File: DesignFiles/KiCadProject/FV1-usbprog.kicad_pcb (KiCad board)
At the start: 2 copper layers, 36 x 32 mm, 8 parts, among them P1 PROG_BUF, U1 74LV4066, U2 CY7C68013A_dev_kit

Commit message: Updated to kicad 5.1, improved compatibility with newer FX2LP boards
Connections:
- U2 pad 10: GND -> Net-(U2-Pad10)
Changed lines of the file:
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@@
-(kicad_pcb (version 4) (host pcbnew "(2015-10-14 BZR 6269, Git 3ca8244)-product")
+(kicad_pcb (version 20171130) (host pcbnew "(5.1.4)-1")
   (general
-    (links 26)
-    (no_connects 0)
-    (area 161.849999 107.099999 198.650001 139.900001)
     (thickness 1.6)
     (drawings 33)
@@
     (zones 0)
     (modules 8)
-    (nets 44)
+    (nets 45)
   )
   (page A4)
@@
     (zone_45_only no)
     (trace_min 0.2)
-    (segment_width 0.2)
-    (edge_width 0.15)
     (via_size 1.6)
     (via_drill 0.6)
@@
     (uvia_min_size 0.2)
     (uvia_min_drill 0.1)
+    (edge_width 0.15)
+    (segment_width 0.2)
     (pcb_text_width 0.3)
     (pcb_text_size 1.5 1.5)
@@
       (layerselection 0x310f0_80000001)
       (usegerberextensions true)
+      (usegerberattributes false)
+      (usegerberadvancedattributes false)
+      (creategerberjobfile false)
       (excludeedgelayer true)
       (linewidth 0.200000)
@@
       (hpglpennumber 1)
       (hpglpenspeed 20)
-      (hpglpendiameter 15)
-      (hpglpenoverlay 2)
+      (hpglpendiameter 15.000000)
       (psnegative false)
       (psa4output false)
@@
       (drillshape 0)
       (scaleselection 1)
-      (outputdirectory I:/Electronics/Projects/Hardware/Gerbers/i2c_buffer/))
+      (outputdirectory "I:/Electronics/Projects/Hardware/Gerbers/i2c_buffer/"))
   )
   (net 0 "")
@@
   (net 42 "Net-(U1-Pad8)")
   (net 43 "Net-(U1-Pad10)")
+  (net 44 "Net-(U2-Pad10)")
   (net_class Default "This is the default net class."
     (clearance 0.25)
@@
     (add_net "Net-(U1-Pad8)")
     (add_net "Net-(U2-Pad1)")
+    (add_net "Net-(U2-Pad10)")
     (add_net "Net-(U2-Pad12)")
     (add_net "Net-(U2-Pad15)")
@@
       (effects (font (size 0.8 0.8) (thickness 0.15)))
     )
-    (fp_text value PROG_BUF (at 2.6 14.79 360) (layer F.Fab)
+    (fp_text value PROG_BUF (at 2.6 14.79) (layer F.Fab)
       (effects (font (size 0.8 0.8) (thickness 0.15)))
     )
@@
       (net 1 /TRG_PWR))
     (model Pin_Headers.3dshapes/Pin_Header_Angled_1x05.wrl
-      (at (xyz 0 -0.2 0))
+      (offset (xyz 0 -5.079999923706055 0))
       (scale (xyz 1 1 1))
       (rotate (xyz 0 0 90))
@@
       (net 2 GND))
     (pad 10 thru_hole circle (at 2.54 10.16) (size 1.8 1.8) (drill 1) (layers *.Cu *.Mask F.SilkS)
-      (net 2 GND))
+      (net 44 "Net-(U2-Pad10)"))
     (pad 11 thru_hole circle (at 0 12.7) (size 1.8 1.8) (drill 1) (layers *.Cu *.Mask F.SilkS)
       (net 2 GND))
@@
       (net 2 GND))
     (model Capacitors_ThroughHole.3dshapes/C_Disc_D3_P2.5.wrl
-      (at (xyz 0.0492126 0 0))
+      (offset (xyz 1.250000021226883 0 0))
       (scale (xyz 1 1 1))
       (rotate (xyz 0 0 0))
@@
     (tags R)
     (autoplace_cost180 10)
-    (fp_text reference R1 (at -1.75 -2 360) (layer F.SilkS)
+    (fp_text reference R1 (at -1.75 -2) (layer F.SilkS)
       (effects (font (size 0.8 0.8) (thickness 0.2032)))
     )

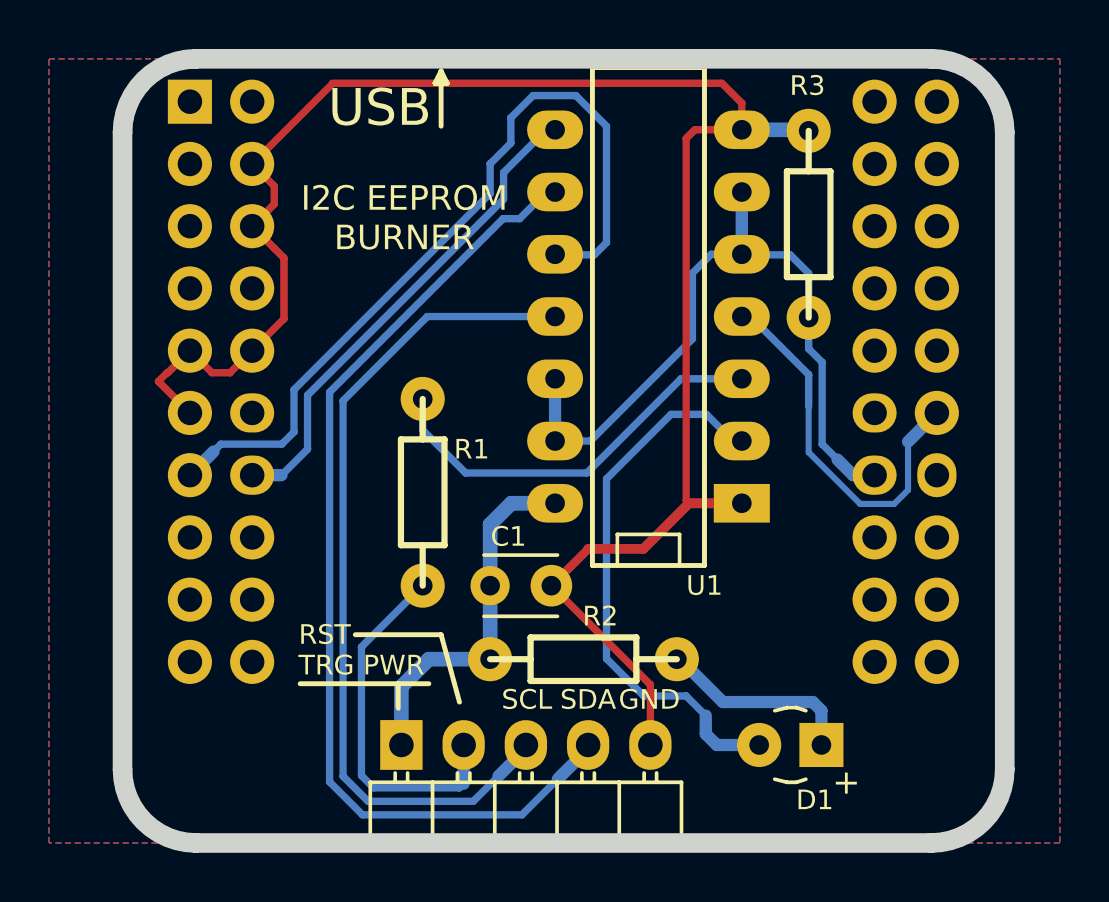
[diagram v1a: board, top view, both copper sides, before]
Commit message: error fixed, cleanup, OshPark link update
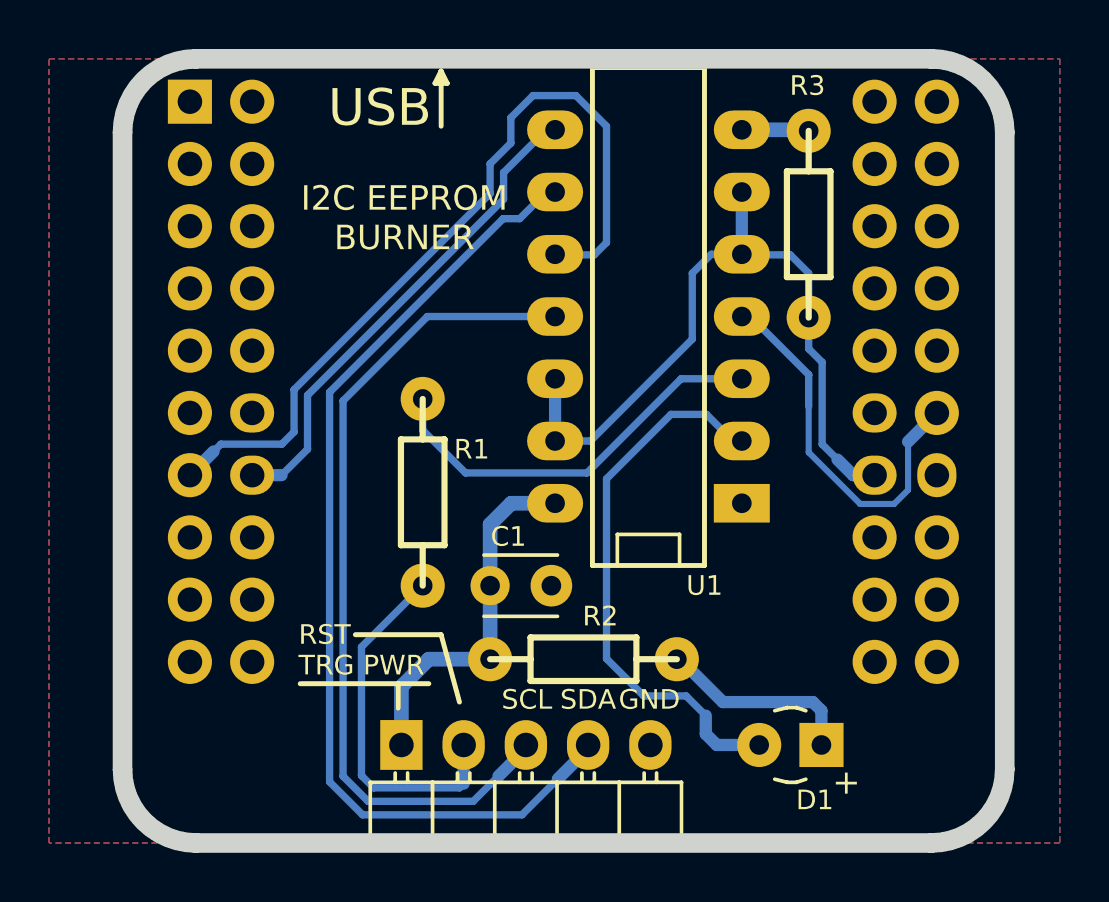
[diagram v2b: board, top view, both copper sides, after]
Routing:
- net GND: track 76.9 -> 3.10 mm
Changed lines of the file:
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@@
     (thickness 1.6)
     (drawings 33)
-    (tracks 144)
+    (tracks 116)
     (zones 0)
     (modules 8)
@@
   (page A4)
   (layers
-    (0 F.Cu signal hide)
+    (0 F.Cu signal)
     (31 B.Cu signal)
     (32 B.Adhes user)
@@
     (38 B.Mask user)
     (39 F.Mask user)
-    (40 Dwgs.User user hide)
+    (40 Dwgs.User user)
     (41 Cmts.User user)
     (42 Eco1.User user)
@@
     (45 Margin user)
     (46 B.CrtYd user)
-    (47 F.CrtYd user hide)
+    (47 F.CrtYd user)
     (48 B.Fab user)
     (49 F.Fab user)
@@
     (visible_elements 7FFFFFFF)
     (pcbplotparams
-      (layerselection 0x310f0_80000001)
+      (layerselection 0x310f0_ffffffff)
       (usegerberextensions true)
       (usegerberattributes false)
@@
       (drillshape 0)
       (scaleselection 1)
-      (outputdirectory "I:/Electronics/Projects/Hardware/Gerbers/i2c_buffer/"))
+      (outputdirectory "../Gerber/"))
   )
   (net 0 "")
@@
   (dimension 11 (width 0.3) (layer Dwgs.User)
     (gr_text "11,000 mm" (at 195 140.9) (layer Dwgs.User)
-      (effects (font (size 1.5 1.5) (thickness 0.3)))
+      (effects (font (size 1 1) (thickness 0.25)))
     )
     (feature1 (pts (xy 189.5 146) (xy 189.5 139.55)))
@@
   (segment (start 179.901744 125.636521) (end 179.546145 125.63652) (width 0.5) (layer B.Cu) (net 1))
   (segment (start 179.961744 125.696521) (end 179.901744 125.636521) (width 0.5) (layer B.Cu) (net 1))
-  (segment (start 181.25 127.5) (end 183.5 127.5) (width 0.4) (layer F.Cu) (net 2))
-  (segment (start 183.5 127.5) (end 185.363479 125.636521) (width 0.4) (layer F.Cu) (net 2))
-  (segment (start 183.79 135.5) (end 183.79 133.04) (width 0.3) (layer F.Cu) (net 2))
-  (segment (start 183.79 133.04) (end 179.75 129) (width 0.3) (layer F.Cu) (net 2))
-  (segment (start 179.75 129) (end 181.25 127.5) (width 0.35) (layer F.Cu) (net 2))
-  (segment (start 185.363479 125.636521) (end 185.25 125.523042) (width 0.3) (layer F.Cu) (net 2))
-  (segment (start 185.25 125.523042) (end 185.25 110.75) (width 0.3) (layer F.Cu) (net 2))
-  (segment (start 185.25 110.75) (end 185.603479 110.396521) (width 0.3) (layer F.Cu) (net 2))
-  (segment (start 185.603479 110.396521) (end 187.521746 110.396521) (width 0.3) (layer F.Cu) (net 2))
-  (segment (start 186.712625 108.5) (end 170.83 108.5) (width 0.3) (layer F.Cu) (net 2))
-  (segment (start 170.83 108.5) (end 167.54 111.79) (width 0.3) (layer F.Cu) (net 2))
-  (segment (start 187.521746 110.396521) (end 187.521746 109.309121) (width 0.3) (layer F.Cu) (net 2))
-  (segment (start 187.521746 109.309121) (end 186.712625 108.5) (width 0.3) (layer F.Cu) (net 2))
-  (segment (start 167.54 114.33) (end 168.439999 113.430001) (width 0.3) (layer F.Cu) (net 2))
-  (segment (start 168.439999 113.430001) (end 168.439999 112.689999) (width 0.3) (layer F.Cu) (net 2))
-  (segment (start 168.439999 112.689999) (end 167.54 111.79) (width 0.3) (layer F.Cu) (net 2))
-  (segment (start 167.54 119.41) (end 168.840001 118.109999) (width 0.3) (layer F.Cu) (net 2))
-  (segment (start 168.840001 118.109999) (end 168.840001 115.630001) (width 0.3) (layer F.Cu) (net 2))
-  (segment (start 168.840001 115.630001) (end 168.439999 115.229999) (width 0.3) (layer F.Cu) (net 2))
-  (segment (start 168.439999 115.229999) (end 167.54 114.33) (width 0.3) (layer F.Cu) (net 2))
-  (segment (start 165 119.41) (end 165.899999 120.309999) (width 0.3) (layer F.Cu) (net 2))
-  (segment (start 165.899999 120.309999) (end 166.640001 120.309999) (width 0.3) (layer F.Cu) (net 2))
-  (segment (start 166.640001 120.309999) (end 167.54 119.41) (width 0.3) (layer F.Cu) (net 2))
-  (segment (start 165 121.95) (end 163.715292 120.665292) (width 0.3) (layer F.Cu) (net 2))
-  (segment (start 164.100001 120.309999) (end 164.070585 120.309999) (width 0.3) (layer F.Cu) (net 2))
-  (segment (start 165 119.41) (end 164.100001 120.309999) (width 0.3) (layer F.Cu) (net 2))
-  (segment (start 164.070585 120.309999) (end 163.715292 120.665292) (width 0.3) (layer F.Cu) (net 2))
-  (segment (start 185.363479 125.636521) (end 187.521746 125.636521) (width 0.4) (layer F.Cu) (net 2))
   (segment (start 187.521746 110.396521) (end 190.206521 110.396521) (width 0.6) (layer B.Cu) (net 2))
   (segment (start 190.206521 110.396521) (end 190.25 110.44) (width 0.6) (layer B.Cu) (net 2))
